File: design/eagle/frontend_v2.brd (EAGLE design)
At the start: 55.9 x 78.7 mm, 39 parts, among them U1 RF3865, U2 ALM32220

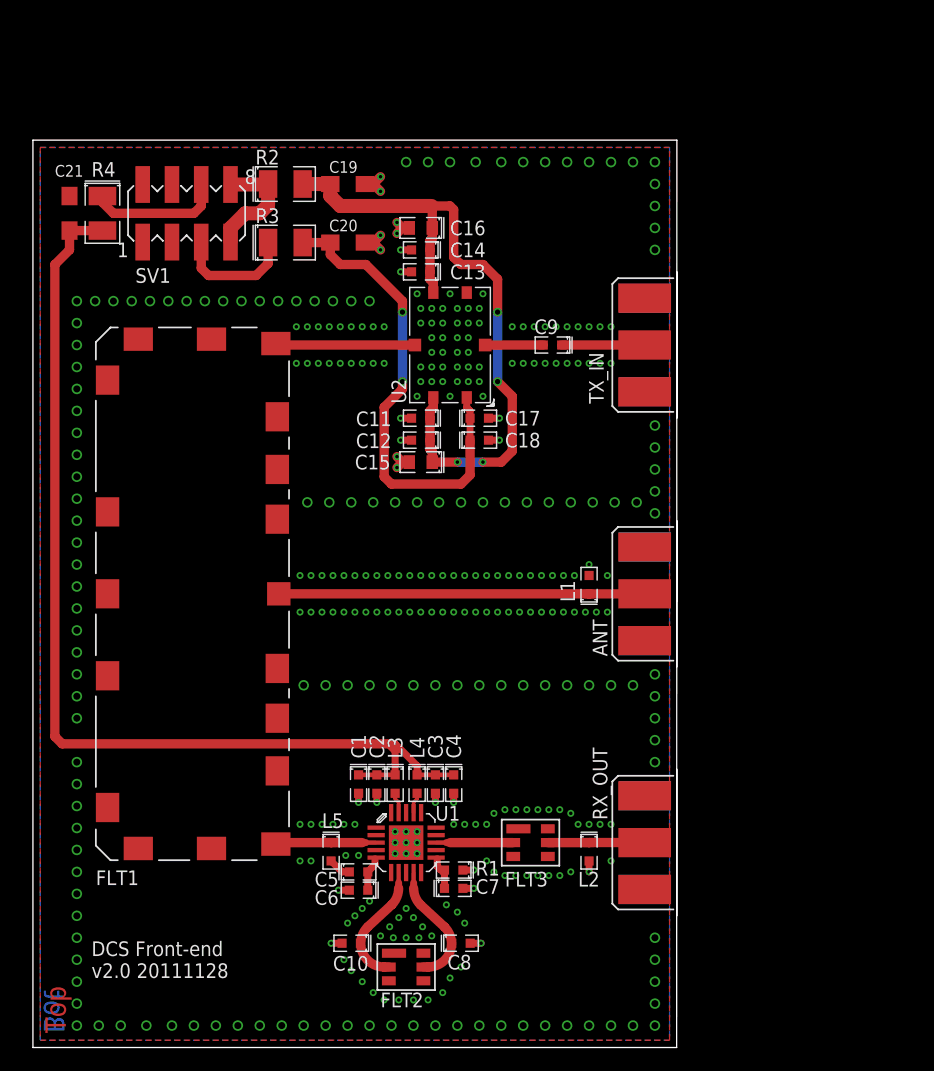
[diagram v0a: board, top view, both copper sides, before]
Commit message: design: Major revision of the PCB to fit into enclosure
Signed-off-by: Sylvain Munaut <tnt@246tNt.com>
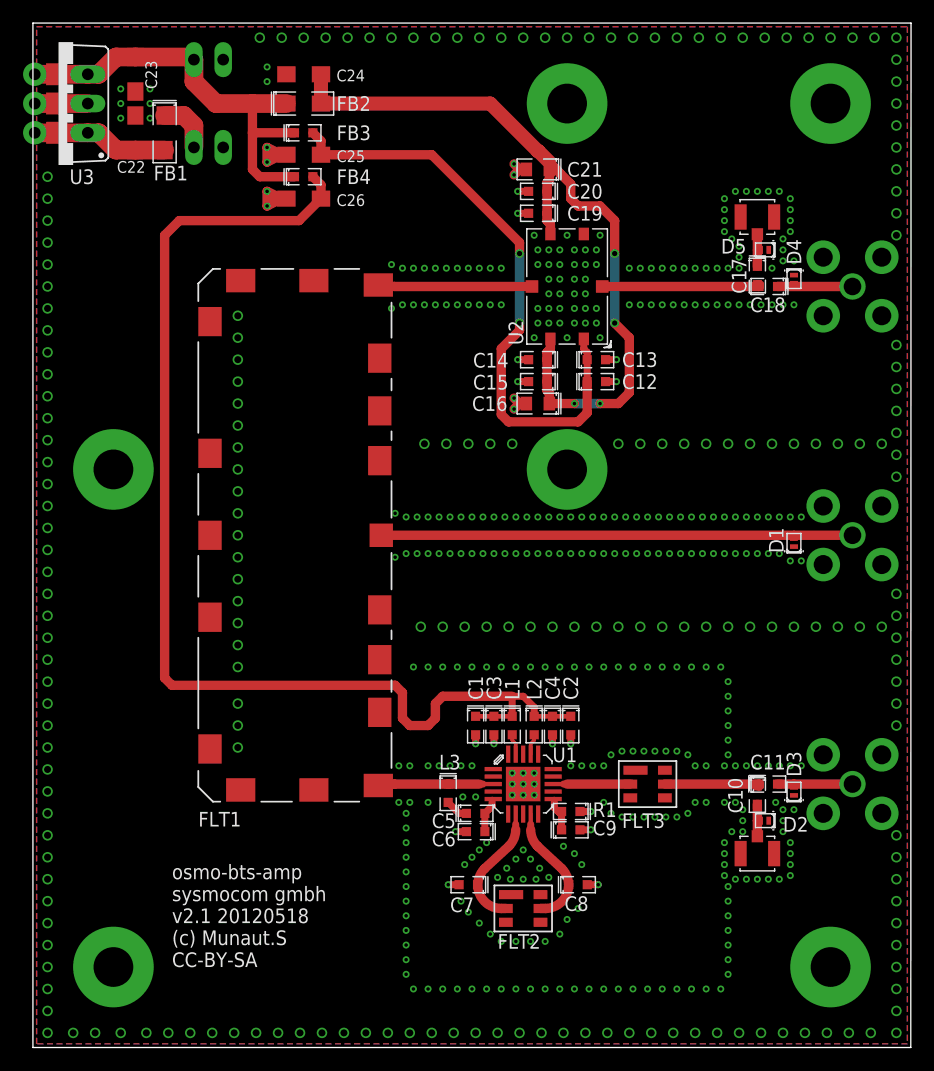
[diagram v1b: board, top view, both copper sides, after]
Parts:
- removed L4, L5: 10n, we_passive:0603
- removed R2, R3, R4: 0R, we_passive:1210
- removed SV1: (no value), con-lstb-tnt:MA04-2_SMD
- added C22, C24, C25, C26: 10u, rcl:SMC_A
- added C23: 22u, rcl:SMC_A
- added D1, D2, D3, D4, D5: PESD5V0F1BL, we_passive:SOD882
- added FB1, FB2: (no value), we_passive:1206
- added FB3, FB4: (no value), we_passive:0603
- added J1: DC_IN, con-molex:6410-02
- added J2: 5V_OUT, con-molex:6410-02
- added RX_OUT_UFL, TX_IN_UFL: (no value), we_conn:HRS_UFL
- added SHLD1: (no value), we_mech:WE-SHC-SMD_25X25
- added U3: MIC29301-5.0BT, we_chips:TO220BV
- ANT, RX_OUT, TX_IN: device we_conn:SMA-F-S-EDGE -> we_conn:SMA-F-S-TH
- C11: value 10n -> 10p
- C14: value 100n -> 10n
- C15: value 2.2u -> 100n; device we_passive:0805 -> we_passive:0603
- C17: value 10n -> DNP
- C18: value 100n -> 10p
- C19: value 47u -> 10n; device rcl:SMC_A -> we_passive:0603
- C2: value 15p -> 10n
- C20: value 47u -> 100n; device rcl:SMC_A -> we_passive:0603
- C21: value 47u -> 2.2u; device rcl:SMC_A -> we_passive:0805
- C4: value 10n -> 15p
- C5: value 100pF -> 100p
- C9: value 10p -> DNP
- L1: value DNP -> 27n
- L2: value DNP -> 10n
- L3: value 27n -> 10n
- moved C11 43.8 mm to (63.8, 22.9), turned to 0 degrees
- moved C9 42.1 mm to (46.7, 18.9), turned to 0 degrees
- moved C21 40.8 mm to (43.8, 76.2), turned to 180 degrees
- moved C10 37.5 mm to (62.9, 21.9), turned to 270 degrees
- moved C18 28.4 mm to (63.8, 66.0), turned to 180 degrees
- moved C17 27.1 mm to (62.9, 67.0), turned to 270 degrees
- moved C16 18.3 mm to (43.8, 55.9)
- moved C2 17.6 mm to (46.7, 27.9)
- moved C20 17.1 mm to (43.8, 74.3), turned to 180 degrees
- moved C13 17.0 mm to (48.9, 59.7), turned to 0 degrees
- moved C19 16.7 mm to (43.8, 72.4), turned to 180 degrees
- moved ANT 16.1 mm to (71.1, 44.5), flipped to the bottom
- moved TX_IN 16.1 mm to (71.1, 66.0), flipped to the bottom
- moved C12 16.1 mm to (48.9, 57.8), turned to 0 degrees
- moved RX_OUT 16.1 mm to (71.1, 22.9), flipped to the bottom
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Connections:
- removed net N$13: R3.1, SV1.5
- removed net N$7: R2.1, SV1.7, SV1.8
- new net 5V: C23.+, FB2.1, FB3.1, FB4.1, J2.1, U3.3
- new net DC_IN: FB1.1, J1.1
- new net DC_IN_FLT: C22.+, FB1.2, U3.1
- new net N$8: C10.2, D2.2, RX_OUT_UFL.SIG
- new net N$9: C10.1, C11.1, FLT3.5
- net 5V_LNA: now also C26.+, FB4.2, L1.1, L2.1; no longer C21.+, L3.1, L4.1, R4.2
- net 5V_PA: now also C19.1, C20.1, C21.1, C24.+, FB2.2; no longer C11.1, C12.1, C13.1, C19.+, R2.2
- net 5V_PACTRL: now also C12.1, C13.1, C25.+, FB3.2; no longer C17.1, C18.1, C20.+, R3.2
- net GND: now also ANT.G1, ANT.G2, ANT.G3, ANT.G4, C19.2, C20.2, C21.2, C22.-, C23.-, C24.-, C25.-, C26.-, C9.2, D1.1, D2.1, D3.1, D4.1, D5.1, J1.2, J2.2, RX_OUT.G1, RX_OUT.G2, RX_OUT.G3, RX_OUT.G4, RX_OUT_UFL.GND@1, RX_OUT_UFL.GND@2, TX_IN.G1, TX_IN.G2, TX_IN.G3, TX_IN.G4, TX_IN_UFL.GND@1, TX_IN_UFL.GND@2, U3.2; no longer ANT.BG1, ANT.BG2, ANT.TG1, ANT.TG2, C10.2, C11.2, C17.2, C18.2, C19.-, C20.-, C21.-, L1.2, L2.2, RX_OUT.BG1, RX_OUT.BG2, RX_OUT.TG1, RX_OUT.TG2, SV1.1, SV1.2, SV1.3, SV1.4, TX_IN.BG1, TX_IN.BG2, TX_IN.TG1, TX_IN.TG2
- net N$1: now also L1.2; no longer L3.2
- net N$10: now also L2.2; no longer L4.2
- net N$14: now also C17.1, D5.2, TX_IN_UFL.SIG; no longer R4.1, SV1.6
- net N$2: now also C18.1, D4.2; no longer C9.1
- net N$3: now also C17.2, C18.2; no longer C9.2
- net N$4: now also L3.2; no longer L5.2
- net N$6: now also C9.1; no longer C7.1
- net RF_ANT: now also D1.2; no longer L1.1
- net RF_UPLINK: now also L3.1; no longer L5.1
- net RF_UPLINK_IS_OUT: now also C7.1; no longer C10.1
- net RF_UPLINK_OUT: now also C11.2, D3.2; no longer FLT3.5, L2.1
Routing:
- net 5V: track 0.00 -> 38.5 mm, vias 0 -> 1
- net DC_IN_FLT: track 0.00 -> 11.9 mm, vias 0 -> 1
- net 5V_LNA: track 89.9 -> 101.6 mm
- net N$13: track 10.6 -> 0.00 mm
- net 5V_PACTRL: track 42.2 -> 52.7 mm
- net N$7: track 10.4 -> 0.00 mm
- net RF_ANT: track 31.8 -> 41.2 mm
- net N$3: track 5.04 -> 13.9 mm
- net N$14: track 11.6 -> 3.06 mm
- net N$9: track 0.00 -> 8.48 mm
- net 5V_PA: track 59.7 -> 68.0 mm
- net GND: track 23.4 -> 31.1 mm, vias 367 -> 597
- net DC_IN: track 0.00 -> 4.80 mm
- net N$8: track 0.00 -> 3.06 mm
- net RF_UPLINK_OUT: track 8.41 -> 6.79 mm
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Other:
- board size 55.9 x 78.7 mm -> 76.2 x 88.9 mm
- board text added: "(c) Munaut.S"
- board text added: "CC-BY-SA"
- board text added: "osmo-bts-amp"
- board text added: "sysmocom gmbh"
- board text added: "v2.1 20120518"
- board text removed: "Bot"
- board text removed: "DCS Front-end"
- board text removed: "Top"
- board text removed: "v2.0 20111128"

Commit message: design: Move the outside holes closer to their optimal position
According to the WAG100 datasheet they should be 36.25 mm from the center
axis. Now they are 36.2 mm from the center axis which should work fine.

Signed-off-by: Sylvain Munaut <tnt@246tNt.com>
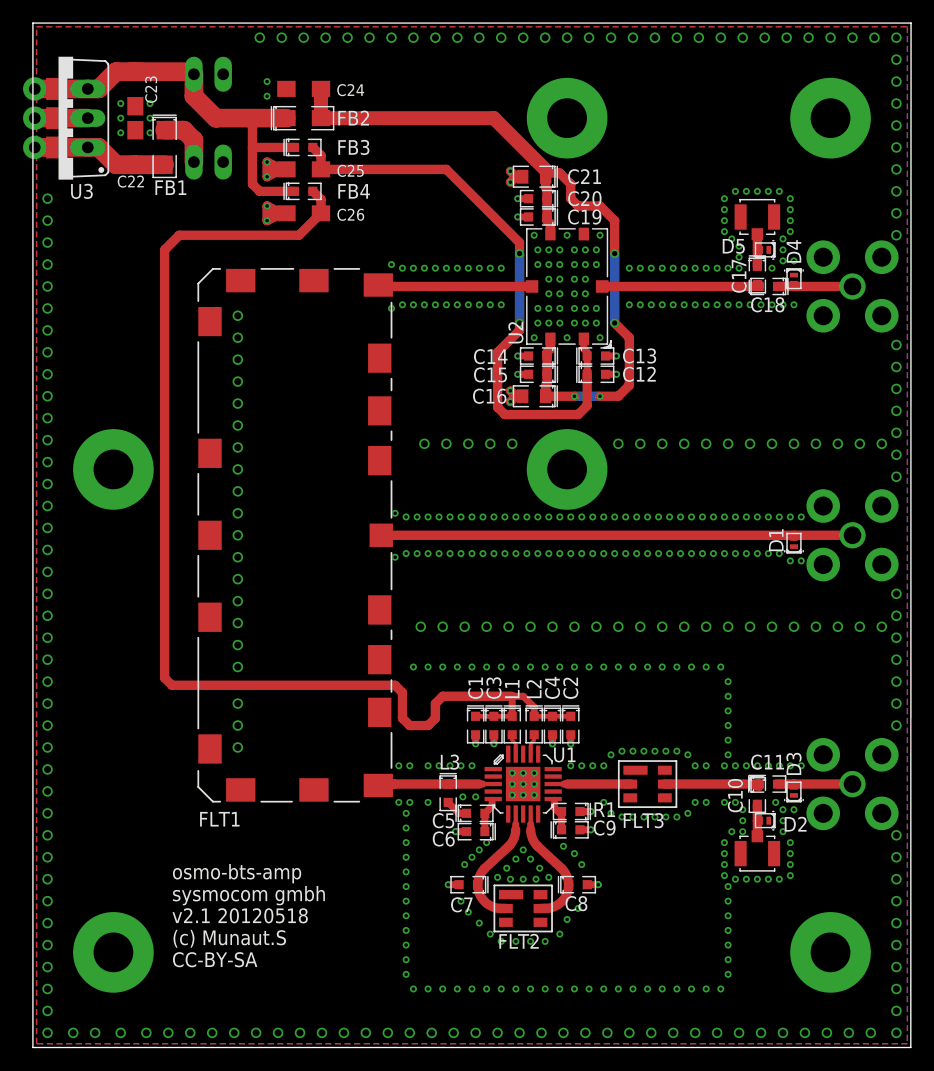
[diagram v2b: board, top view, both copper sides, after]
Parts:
- moved FB2 1.27 mm to (23.5, 80.6)
- moved J1 1.27 mm to (15.2, 76.8)
- moved U3 1.27 mm to (2.22, 80.6)
- moved C22 1.27 mm to (8.89, 78.1)
- moved C23 1.27 mm to (8.89, 83.2)
- moved C24 1.27 mm to (23.5, 83.2)
- moved C25 1.27 mm to (23.5, 76.2)
- moved C26 1.27 mm to (23.5, 72.4)
- moved FB1 1.27 mm to (11.4, 78.1)
- moved FB3 1.27 mm to (23.5, 78.1)
- moved FB4 1.27 mm to (23.5, 74.3)
- moved J2 1.27 mm to (15.2, 84.5)
- moved C21 0.71 mm to (43.5, 75.6)
- moved C16 0.71 mm to (43.5, 56.5)
- moved C12 0.64 mm to (48.9, 58.4)
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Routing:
- net 5V_PA: track 68.0 -> 65.6 mm
- net 5V_PACTRL: track 52.7 -> 51.4 mm
- net 5V_LNA: track 101.6 -> 100.4 mm
- net GND: vias 597 -> 596

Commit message: design: Make the traces 40 mil wide with 12 mil GND separaton
This should keep a ~ 55 ohm impedance (close enough)

Signed-off-by: Sylvain Munaut <tnt@246tNt.com>
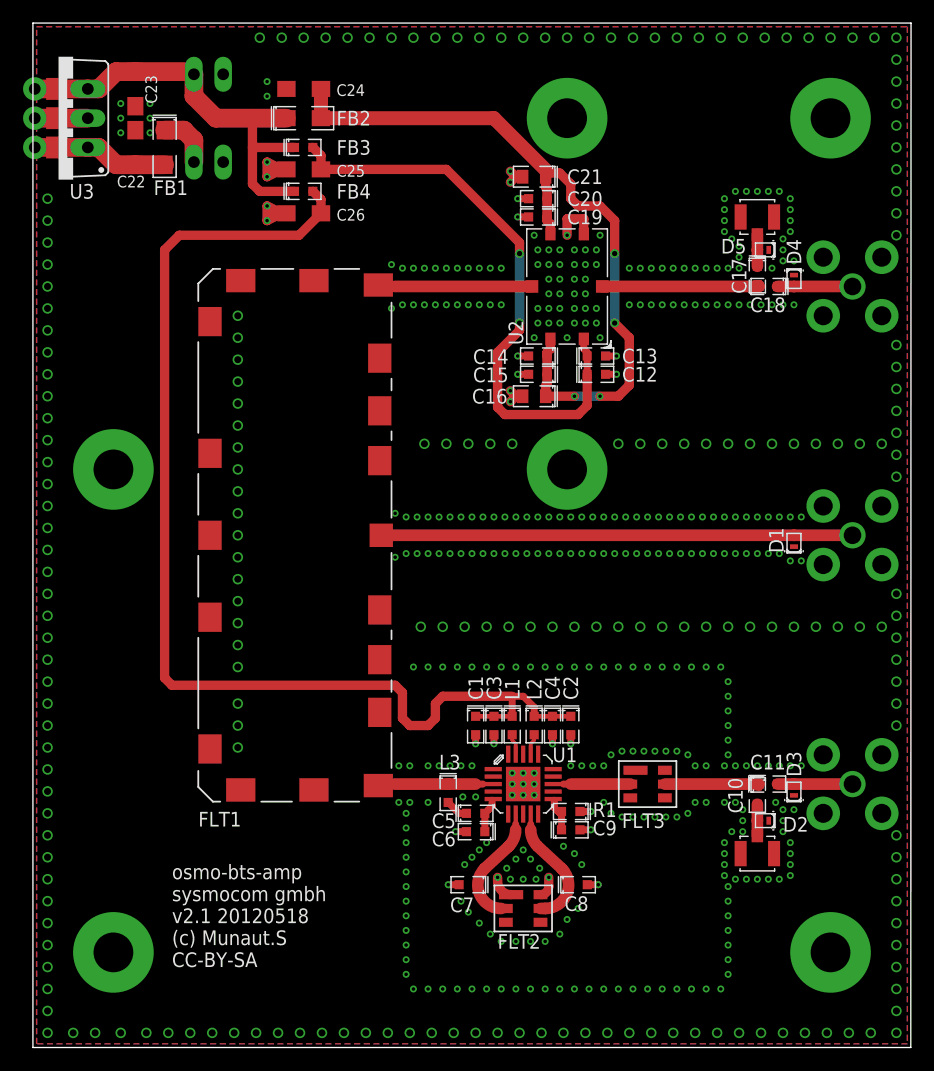
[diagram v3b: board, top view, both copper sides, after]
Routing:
- net GND: track 31.1 -> 39.0 mm
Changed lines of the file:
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@@
 <text x="12.065" y="14.605" size="1.27" layer="25">osmo-bts-amp</text>
 <text x="12.065" y="10.795" size="1.27" layer="25">v2.1 20120518</text>
-<rectangle x1="41.91" y1="10.16" x2="43.4975" y2="13.97" layer="41"/>
+<rectangle x1="41.91" y1="10.16" x2="43.4975" y2="13.335" layer="41"/>
 <rectangle x1="41.5925" y1="10.16" x2="41.91" y2="10.4775" layer="41"/>
 <rectangle x1="52.705" y1="20.955" x2="54.61" y2="24.765" layer="41"/>
@@
 <via x="1.27" y="62.23" extent="1-16" drill="0.6096"/>
 <via x="17.78" y="57.785" extent="1-16" drill="0.6096"/>
-<polygon width="0.4064" layer="1" isolate="0.2032">
+<polygon width="0.4064" layer="1" isolate="0.3048">
 <vertex x="75.8825" y="0.3175"/>
 <vertex x="0.3175" y="0.3175"/>
@@
 <via x="1.27" y="66.04" extent="1-16" drill="0.6096"/>
 <via x="1.27" y="67.945" extent="1-16" drill="0.6096"/>
-<wire x1="1.27" y1="68.58" x2="1.27" y2="68.58" width="0" layer="19" extent="1-16"/>
 <via x="1.27" y="69.85" extent="1-16" drill="0.6096"/>
 <via x="1.27" y="71.755" extent="1-16" drill="0.6096"/>
@@
 <via x="17.78" y="27.94" extent="1-16" drill="0.6096"/>
 <via x="17.78" y="26.035" extent="1-16" drill="0.6096"/>
+<wire x1="41.495" y1="13.265" x2="40.3225" y2="14.4375" width="0.8128" layer="1" curve="-90"/>
+<wire x1="40.3225" y1="14.4375" x2="40.3225" y2="14.7638" width="0.8128" layer="1"/>
+<wire x1="44.045" y1="13.265" x2="44.7675" y2="13.9875" width="0.8128" layer="1" curve="90"/>
+<wire x1="44.7675" y1="13.9875" x2="44.7675" y2="14.7638" width="0.8128" layer="1"/>
+<wire x1="47.805" y1="70.59" x2="47.805" y2="71.91375" width="0.8128" layer="1"/>
+<wire x1="47.805" y1="71.91375" x2="46.355" y2="71.91375" width="0.8128" layer="1"/>
+<wire x1="46.355" y1="71.91375" x2="46.355" y2="70.485" width="0.8128" layer="1"/>
 </signal>
 <signal name="RF_ANT">
 <contactref element="FLT1" pad="ANT"/>
-<wire x1="30.226" y1="44.45" x2="66.04" y2="44.45" width="0.8128" layer="1"/>
+<wire x1="30.226" y1="44.45" x2="66.04" y2="44.45" width="1.016" layer="1"/>
 <contactref element="ANT" pad="C"/>
 <contactref element="D1" pad="2"/>
 <wire x1="66.04" y1="44.165" x2="66.04" y2="44.45" width="0.3048" layer="1"/>
-<wire x1="71.12" y1="44.45" x2="66.04" y2="44.45" width="0.8128" layer="1"/>
+<wire x1="71.12" y1="44.45" x2="66.04" y2="44.45" width="1.016" layer="1"/>
 </signal>
 <signal name="RF_DOWNLINK">
 <contactref element="FLT1" pad="HI"/>
 <contactref element="U2" pad="5"/>
-<wire x1="31.369" y1="66.04" x2="43.305" y2="66.04" width="0.8128" layer="1"/>
+<wire x1="31.369" y1="66.04" x2="43.305" y2="66.04" width="1.016" layer="1"/>
 <wire x1="29.972" y1="66.167" x2="31.369" y2="66.04" width="0.8128" layer="1"/>
 </signal>
@@
 <contactref element="L3" pad="1"/>
 <wire x1="39.0526" y1="22.86" x2="39.945" y2="22.86" width="0.3048" layer="1"/>
-<wire x1="38.735" y1="22.86" x2="39.0526" y2="22.86" width="0.6096" layer="1"/>
-<wire x1="36.0363" y1="22.86" x2="38.735" y2="22.86" width="0.8128" layer="1"/>
+<wire x1="38.4175" y1="22.86" x2="39.0526" y2="22.86" width="0.6096" layer="1"/>
+<wire x1="36.0363" y1="22.86" x2="38.4175" y2="22.86" width="1.016" layer="1"/>
 <wire x1="36.0363" y1="22.86" x2="36.0363" y2="22.8662" width="0.8128" layer="1"/>
-<wire x1="31.369" y1="22.86" x2="36.0363" y2="22.86" width="0.8128" layer="1"/>
+<wire x1="31.369" y1="22.86" x2="36.0363" y2="22.86" width="1.016" layer="1"/>
 <wire x1="29.972" y1="22.733" x2="31.369" y2="22.86" width="0.8128" layer="1"/>
 </signal>
@@
 <wire x1="41.895" y1="19.3826" x2="41.895" y2="20.26" width="0.3048" layer="1"/>
 <wire x1="41.895" y1="18.9063" x2="41.895" y2="19.3826" width="0.6096" layer="1"/>
-<wire x1="41.2998" y1="17.4696" x2="41.895" y2="18.9063" width="0.8128" layer="1" curve="44.998839"/>
+<wire x1="41.2998" y1="17.4696" x2="41.895" y2="18.9063" width="1.016" layer="1" curve="44.998839"/>
 <wire x1="40.64" y1="12.0651" x2="41.045" y2="12.065" width="0.8128" layer="1"/>
-<wire x1="39.2032" y1="15.5339" x2="40.64" y2="12.0651" width="0.8128" layer="1" curve="135.000677"/>
-<wire x1="39.2032" y1="15.5339" x2="41.2998" y2="17.4696" width="0.8128" layer="1"/>
+<wire x1="39.2032" y1="15.5339" x2="40.64" y2="12.0651" width="1.016" layer="1" curve="135.000677"/>
+<wire x1="39.2032" y1="15.5339" x2="41.2998" y2="17.4696" width="1.016" layer="1"/>
 <wire x1="38.5825" y1="14.1288" x2="39.2032" y2="15.5339" width="0.2032" layer="1"/>
 </signal>
@@
 <contactref element="U1" pad="9"/>
 <contactref element="C8" pad="1"/>
-<wire x1="44.045" y1="12.065" x2="44.45" y2="12.0651" width="0.8128" layer="1"/>
-<wire x1="44.45" y1="12.0651" x2="45.8868" y2="15.5339" width="0.8128" layer="1" curve="135.000677"/>
+<wire x1="44.045" y1="12.065" x2="44.45" y2="12.0651" width="1.016" layer="1"/>
+<wire x1="44.45" y1="12.0651" x2="45.8868" y2="15.5339" width="1.016" layer="1" curve="135.000677"/>
 <wire x1="43.195" y1="19.3826" x2="43.195" y2="20.26" width="0.3048" layer="1"/>
 <wire x1="43.1951" y1="18.9065" x2="43.195" y2="19.3826" width="0.6096" layer="1"/>
-<wire x1="43.7902" y1="17.4696" x2="43.1951" y2="18.9065" width="0.8128" layer="1" curve="-45.000975"/>
-<wire x1="45.8868" y1="15.5339" x2="43.7902" y2="17.4696" width="0.8128" layer="1"/>
+<wire x1="43.7902" y1="17.4696" x2="43.1951" y2="18.9065" width="1.016" layer="1" curve="-45.000975"/>
+<wire x1="45.8868" y1="15.5339" x2="43.7902" y2="17.4696" width="1.016" layer="1"/>
 <wire x1="45.8868" y1="15.5339" x2="46.5075" y2="14.1289" width="0.2032" layer="1"/>
 </signal>
@@
 <contactref element="FLT3" pad="2"/>
 <wire x1="45.145" y1="22.86" x2="46.0375" y2="22.86" width="0.3048" layer="1"/>
-<wire x1="46.0375" y1="22.86" x2="46.355" y2="22.86" width="0.6096" layer="1"/>
-<wire x1="46.355" y1="22.86" x2="51.84" y2="22.86" width="0.8128" layer="1"/>
+<wire x1="46.0375" y1="22.86" x2="46.6725" y2="22.86" width="0.6096" layer="1"/>
+<wire x1="46.6725" y1="22.86" x2="51.84" y2="22.86" width="1.016" layer="1"/>
 </signal>
 <signal name="RF_UPLINK_OUT">
@@
 <contactref element="C11" pad="2"/>
 <contactref element="D3" pad="2"/>
-<wire x1="64.6175" y1="22.86" x2="66.04" y2="22.86" width="0.8128" layer="1"/>
-<wire x1="66.04" y1="22.86" x2="71.12" y2="22.86" width="0.8128" layer="1"/>
+<wire x1="64.6175" y1="22.86" x2="66.04" y2="22.86" width="1.016" layer="1"/>
+<wire x1="66.04" y1="22.86" x2="71.12" y2="22.86" width="1.016" layer="1"/>
 <wire x1="66.04" y1="22.575" x2="66.04" y2="22.86" width="0.3048" layer="1"/>
 </signal>
@@
 <contactref element="D4" pad="2"/>
 <wire x1="66.04" y1="66.325" x2="66.04" y2="66.04" width="0.3048" layer="1"/>
-<wire x1="66.04" y1="66.04" x2="64.6175" y2="66.04" width="0.8128" layer="1"/>
-<wire x1="71.12" y1="66.04" x2="66.04" y2="66.04" width="0.8128" layer="1"/>
+<wire x1="66.04" y1="66.04" x2="64.6175" y2="66.04" width="1.016" layer="1"/>
+<wire x1="71.12" y1="66.04" x2="66.04" y2="66.04" width="1.016" layer="1"/>
 </signal>
 <signal name="N$3">
@@
 <wire x1="62.865" y1="66.1925" x2="63.0175" y2="66.1925" width="0.8128" layer="1"/>
 <wire x1="63.0175" y1="66.1925" x2="63.0175" y2="66.04" width="0.8128" layer="1"/>
-<wire x1="49.405" y1="66.04" x2="63.0175" y2="66.04" width="0.8128" layer="1"/>
+<wire x1="49.405" y1="66.04" x2="63.0175" y2="66.04" width="1.016" layer="1"/>
 </signal>
 <signal name="5V_PA">
@@
 <contactref element="D2" pad="2"/>
 <wire x1="63.15" y1="19.685" x2="62.865" y2="19.685" width="0.3048" layer="1"/>
-<wire x1="62.865" y1="19.685" x2="62.865" y2="21.1075" width="0.8128" layer="1"/>
-<wire x1="62.865" y1="19.685" x2="62.865" y2="18.33" width="0.8128" layer="1"/>
+<wire x1="62.865" y1="19.685" x2="62.865" y2="21.1075" width="1.016" layer="1"/>
+<wire x1="62.865" y1="19.685" x2="62.865" y2="18.33" width="1.016" layer="1"/>
 </signal>
 <signal name="N$9">
@@
 <contactref element="C11" pad="1"/>
 <contactref element="FLT3" pad="5"/>
-<wire x1="54.84" y1="22.86" x2="63.0175" y2="22.86" width="0.8128" layer="1"/>
+<wire x1="54.84" y1="22.86" x2="63.0175" y2="22.86" width="1.016" layer="1"/>
 <wire x1="62.865" y1="22.7075" x2="63.0175" y2="22.7075" width="0.8128" layer="1"/>
 <wire x1="63.0175" y1="22.7075" x2="63.0175" y2="22.86" width="0.8128" layer="1"/>
@@
 <contactref element="C17" pad="1"/>
 <wire x1="63.15" y1="69.215" x2="62.865" y2="69.215" width="0.3048" layer="1"/>
-<wire x1="62.865" y1="69.215" x2="62.865" y2="70.57" width="0.8128" layer="1"/>
-<wire x1="62.865" y1="69.215" x2="62.865" y2="67.7925" width="0.8128" layer="1"/>
+<wire x1="62.865" y1="69.215" x2="62.865" y2="70.57" width="1.016" layer="1"/>
+<wire x1="62.865" y1="69.215" x2="62.865" y2="67.7925" width="1.016" layer="1"/>
 </signal>
 </signals>
